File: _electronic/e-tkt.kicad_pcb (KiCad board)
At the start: 6 copper layers, 99.6 x 76.2 mm, 158 parts

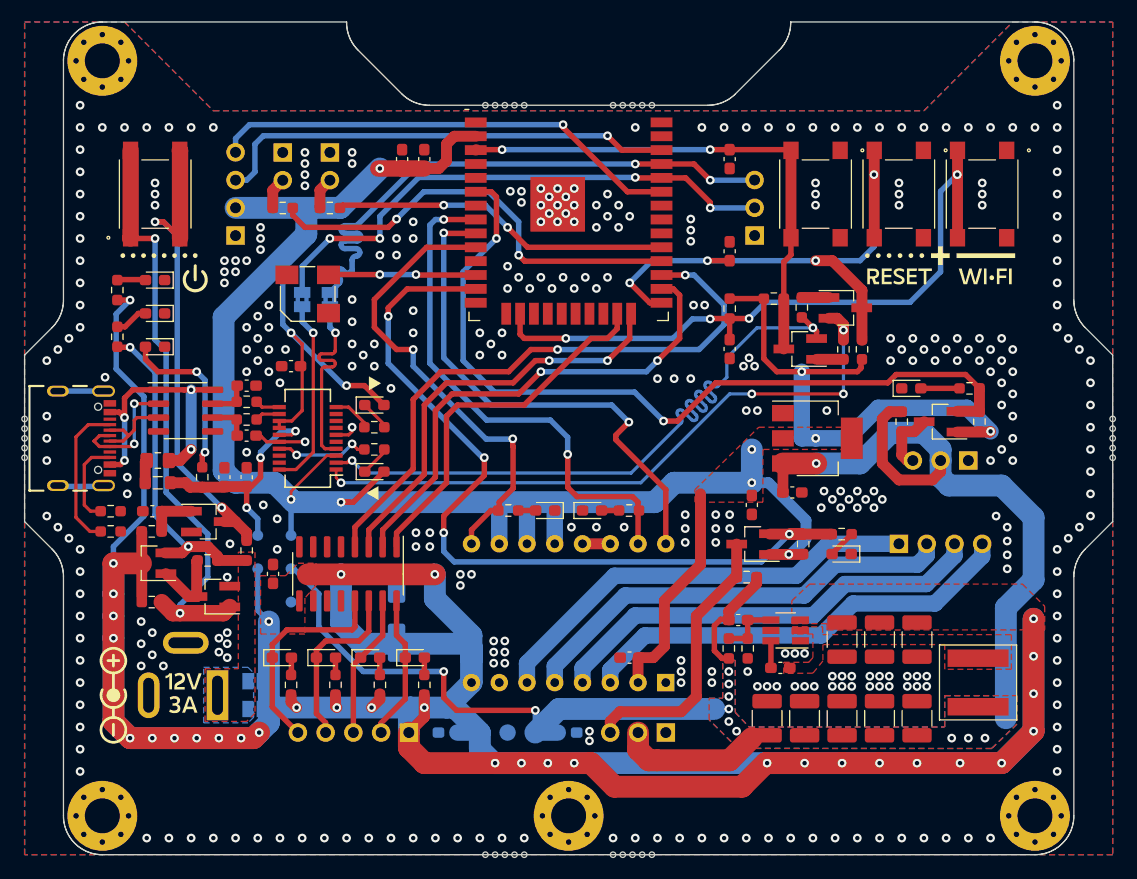
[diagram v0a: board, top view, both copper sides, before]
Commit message: revised pcb: direct power, leds, ftdi w/o 3v3
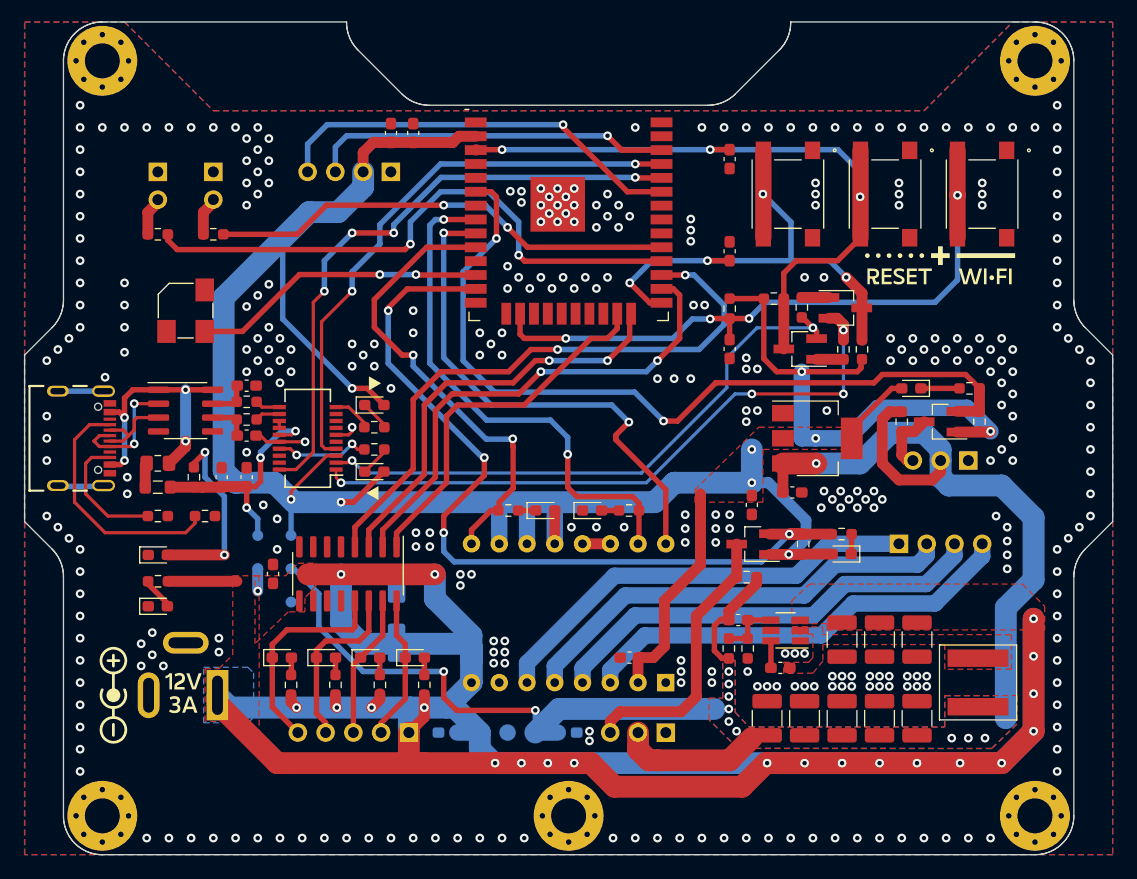
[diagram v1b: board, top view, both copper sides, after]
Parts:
- removed ? (x30): , 
- removed C_POW3: 22uF 12V 1mOhm, Capacitor_SMD:C_0603_1608Metric_Pad1.08x0.95mm_HandSolder
- removed C_SER1: 0.1uF 10V, Capacitor_SMD:C_0603_1608Metric_Pad1.08x0.95mm_HandSolder
- removed D_POW1: LED white, LED_SMD:LED_0603_1608Metric_Pad1.05x0.95mm_HandSolder
- removed JP1, JP2: SolderJumper_2_Open, Jumper:SolderJumper-2_P1.3mm_Open_Pad1.0x1.5mm
- removed JP_SER1, JP_SER3: Bridged, Jumper:SolderJumper-2_P1.3mm_Bridged2Bar_Pad1.0x1.5mm
- removed J_EXT1: Conn_01x03_Male, Connector_PinHeader_2.54mm:PinHeader_1x03_P2.54mm_Horizontal
- removed Q_POW1: SQ2351ES-T1_GE3, Package_TO_SOT_SMD:SOT-23_Handsoldering
- removed Q_POW2, Q_POW3: MMBT3904,215, Package_TO_SOT_SMD:SOT-23_Handsoldering
- removed R_POW1: 430R, Resistor_SMD:R_0603_1608Metric_Pad0.98x0.95mm_HandSolder
- removed R_POW2, R_POW3, R_POW5: 100K, Resistor_SMD:R_0603_1608Metric_Pad0.98x0.95mm_HandSolder
- removed R_POW4: 1M, Resistor_SMD:R_0603_1608Metric_Pad0.98x0.95mm_HandSolder
- removed SW_POW1: B3FS-1000, b3fs:B3FS-1000
- C_ENA1, C_MCU1, C_RST1, C_SER4, C_WIFI1: value 0.1uF 10V -> 0.1uF 50V
- L1: value ~ -> SRP6060FA-100M
- moved D_POW2 29.8 mm to (140.7, -174.1), turned to 0 degrees
- moved R_POW6 26.9 mm to (140.7, -176.4), turned to 180 degrees
- moved D_USB1 19.1 mm to (140.7, -178.8), turned to 0 degrees
- moved J_OLED1 15.4 mm to (162.0, -213.9), turned to 90 degrees
- moved R_LEDP1 11.7 mm to (140.7, -208.2)
- moved J_LEDP1 11.6 mm to (140.7, -213.9)
- moved LS1 11.3 mm to (143.3, -201.2), turned to 90 degrees
- moved R_LEDE1 10.9 mm to (145.8, -208.2)
- moved J_LEDE1 10.8 mm to (145.8, -213.9)
- moved SW_RST1 10.1 mm to (198.4, -211.8)
- moved R_USB1 8.75 mm to (145.0, -182.4)
- moved SW_ENA1 6.36 mm to (207.3, -211.8)
- moved R_USB2 4.34 mm to (140.7, -182.4)
- moved C_MCU2 2.59 mm to (162.1, -217.4)
- moved C_MCU1 2.59 mm to (164.1, -217.4)
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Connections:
- D_HALL1 pad 1: GNDREF -> Net-(R_HALL3-Pad2)
- D_HALL1 pad 2: Net-(D_HALL1-Pad2) -> +3.3V
- D_NEMA1 pad 1: GNDREF -> Net-(R_NEMA1-Pad2)
- D_NEMA1 pad 2: Net-(D_NEMA1-Pad2) -> +3.3V
- D_SERVO1 pad 1: GNDREF -> Net-(D_SERVO1-Pad1)
- D_SERVO1 pad 2: Net-(D_SERVO1-Pad2) -> +3.3V
- J_POW1 pad 1: Net-(J_POW1-Pad1) -> +12V
- R_HALL3 pad 2: Net-(D_HALL1-Pad2) -> Net-(R_HALL3-Pad2)
- R_NEMA1 pad 2: Net-(D_NEMA1-Pad2) -> Net-(R_NEMA1-Pad2)
- R_SERVO3 pad 2: Net-(D_SERVO1-Pad2) -> Net-(D_SERVO1-Pad1)
- U_SER1 pad 13: +3.3V -> Net-(U_SER1-Pad13)
- U_SER1 pad 14: +3.3V -> Net-(U_SER1-Pad13)
- U_SER1 pad 20: Net-(JP_SER3-Pad1) -> IO3 RXD
- U_SER1 pad 4: Net-(JP_SER1-Pad1) -> IO1 TXD
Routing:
- net +12V: track 327.3 -> 252.4 mm, vias 34 -> 22
- net Net-(Q_POW2-Pad1): track 54.6 -> 0.00 mm, vias 2 -> 0
- net Net-(Q_POW3-Pad3): track 45.1 -> 0.00 mm, vias 2 -> 0
- net Net-(J_POW1-Pad1): track 30.2 -> 0.00 mm, vias 2 -> 0
- net Net-(JP_SER1-Pad1): track 17.8 -> 0.00 mm, vias 1 -> 0
- net Net-(JP_SER3-Pad1): track 17.5 -> 0.00 mm, vias 1 -> 0
- net EN: track 47.5 -> 63.4 mm, vias 2 -> 3
- net /MCU/IO27 BUZZER OUT: track 13.5 -> 27.0 mm
- net IO17 LED PRESS: track 40.6 -> 53.9 mm
- net IO5 LED END: track 31.1 -> 42.8 mm
- net RTS: track 63.5 -> 53.8 mm
- net IO22 OLED SCL: track 42.7 -> 33.1 mm
- net Net-(J_USB1-PadA5): track 13.7 -> 22.7 mm
- net Net-(Q_POW1-Pad1): track 7.06 -> 0.00 mm
- net IO3 RXD: track 49.8 -> 56.2 mm
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- added copper zone on B.Cu, net +12V
- removed copper zone on B.Cu, net Net-(J_POW1-Pad1)
- removed copper zone on F.Cu, net Net-(J_POW1-Pad1)
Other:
- board text added: "LED END"
- board text added: "LED PRESS"
- board text removed: "END"
- board text removed: "EXTERNAL ! 3V3 ! FLASHING"
- board text removed: "LEDS"
- board text removed: "PRESS"
- board text removed: "RX EXT"
- board text removed: "TX EXT"

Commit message: adjusts on pcb layout and visual id
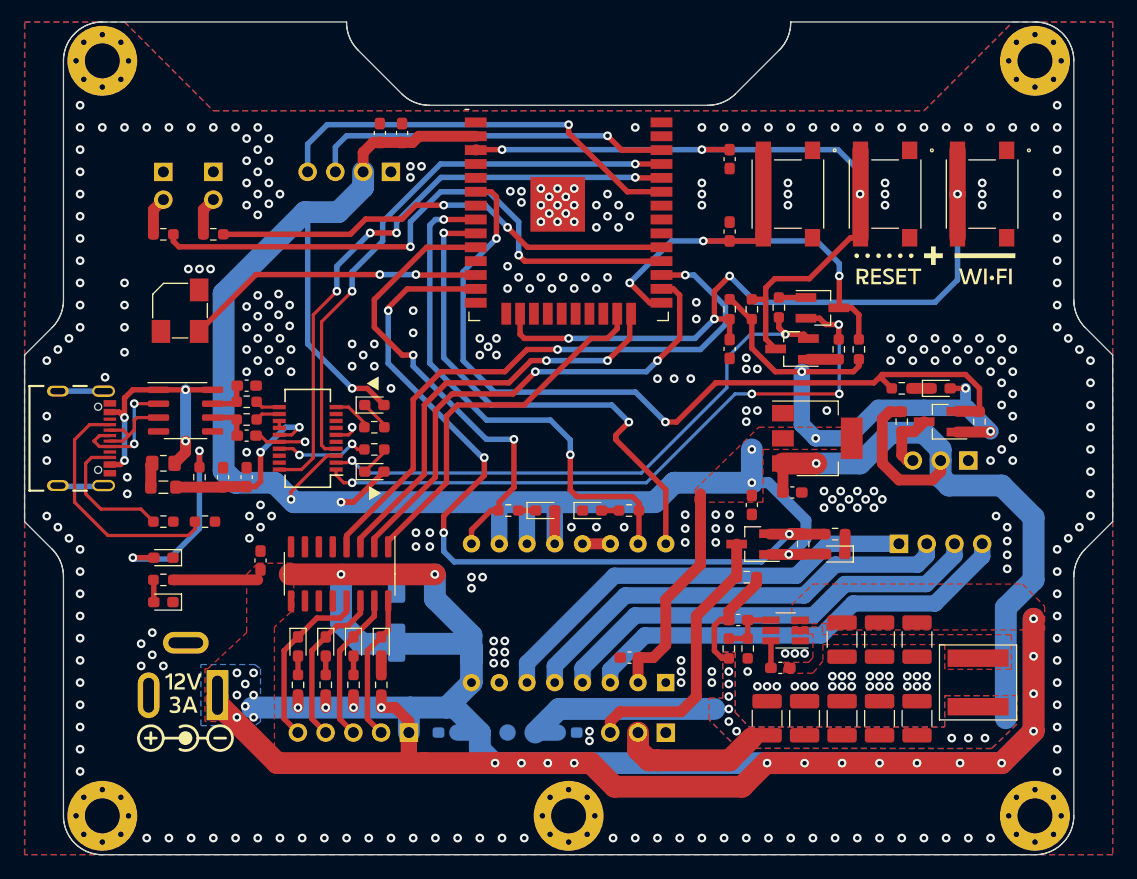
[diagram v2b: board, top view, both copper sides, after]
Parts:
- removed the G*** at (178.3, -189.5) (x3)
- removed TP_12v1, TP_3.3v1, TP_5v1, TP_6v1, TP_GND3: TestPoint, TestPoint:TestPoint_Pad_D1.0mm
- added G*** (x3): LOGO, LOGO, F.Cu at (178.3, -189.5)
- added G***: LOGO, LOGO, B.Cu at (178.3, -191.3)
- added REF**: OSHW-Symbol_6.7x6mm_SilkScreen, Symbol:OSHW-Symbol_6.7x6mm_SilkScreen, B.Cu at (178.3, -198.9)
- moved R_HALL3 6.20 mm to (208.8, -194.1), turned to 0 degrees
- moved R_STP1 3.94 mm to (161.2, -166.9)
- moved D_STP1 3.23 mm to (161.2, -170.4), turned to -90 degrees
- moved D_HALL1 2.68 mm to (212.3, -194.1), turned to 0 degrees
- moved R_STP2 2.41 mm to (158.6, -166.9)
- moved R_ENA1 2.24 mm to (195.1, -201.3), turned to -90 degrees
- moved R_AUTO2 2.10 mm to (197.5, -201.5)
- moved Q_AUTO2 2.10 mm to (201.5, -201.4)
- moved D_STP2 1.83 mm to (158.6, -170.4), turned to -90 degrees
- moved C_RST1 1.80 mm to (193.0, -208.4)
- moved D_STP4 1.79 mm to (153.5, -170.4), turned to -90 degrees
- moved C_STP1 1.68 mm to (150.1, -178.3)
- moved D_STP3 1.02 mm to (156.1, -170.4), turned to -90 degrees
- moved C_MCU1 1.02 mm to (163.1, -217.4)
- moved C_MCU2 1.02 mm to (161.0, -217.4)
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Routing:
- net +6V: track 140.2 -> 107.3 mm, vias 12 -> 10
- net +3.3V: track 240.6 -> 232.2 mm, vias 9 -> 10
- net IO13 WIFI RST: track 62.0 -> 66.9 mm
- net VBUS: track 21.7 -> 17.3 mm, vias 3 -> 2
- net Net-(D_STP4-Pad1): track 19.6 -> 16.2 mm
- net EN: track 63.4 -> 66.5 mm
- net +12V: track 252.4 -> 250.3 mm, vias 22 -> 29
- net Net-(R_HALL3-Pad2): track 3.54 -> 1.77 mm
- net IO34 HALL: track 74.4 -> 76.1 mm
- net DTR: track 59.6 -> 61.0 mm
- net RTS: track 53.8 -> 52.4 mm
- net Net-(D_STP3-Pad1): track 16.2 -> 15.0 mm
- net IO0 RESET: track 48.5 -> 47.3 mm, vias 4 -> 3
- net Net-(D_POW2-Pad2): track 3.02 -> 2.05 mm
- net Net-(D_STP2-Pad1): track 13.2 -> 14.1 mm
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- removed copper zone on In3.Cu, net +12V
- removed copper zone on In4.Cu, net GNDREF
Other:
- copper layers 6 -> 4
- board text added: "2022/09/21"
- board text added: "BR000010"
- board text added: "v1.0"
- board text removed: "12V"
- board text removed: "2022/07/21"
- board text removed: "3.3V"
- board text removed: "5V USB"
- board text removed: "v0.9"
